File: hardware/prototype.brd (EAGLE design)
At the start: 62.2 x 57.2 mm, 32 parts, among them Q3 BS170

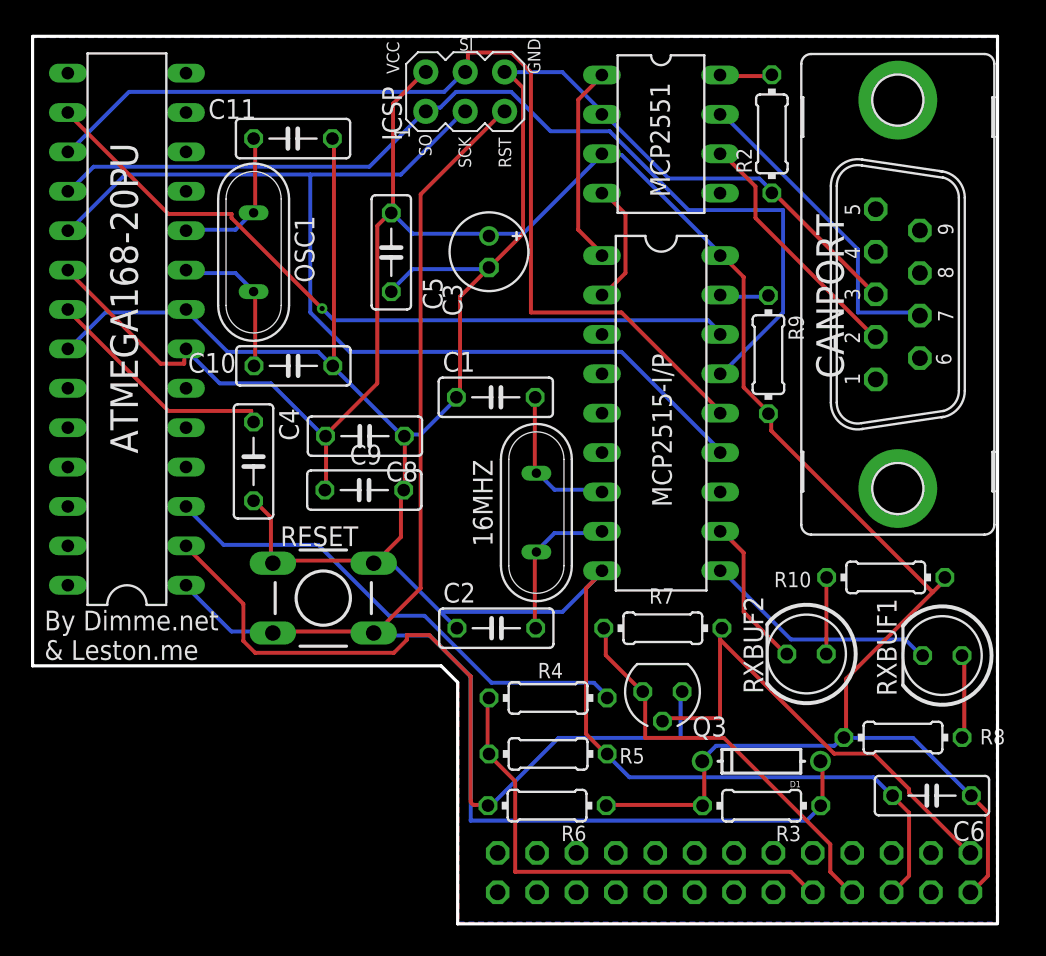
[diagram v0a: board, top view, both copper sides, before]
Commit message: Added gerbers for DirtyPCBs and OSHpark.
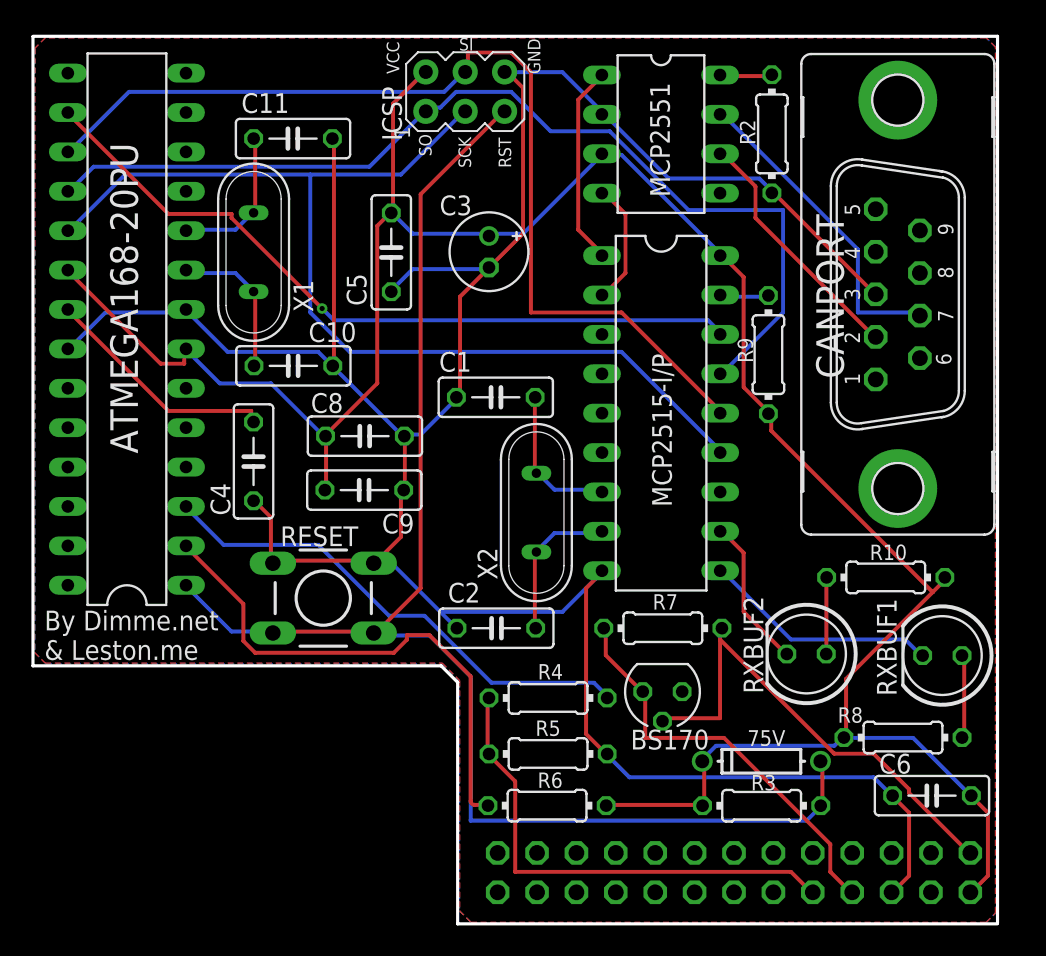
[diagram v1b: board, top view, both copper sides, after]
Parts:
- BS170: value BS170 -> (none)
- C1, C10, C11, C2: value (none) -> 22p
- C3: value (none) -> 10u
- C4, C5, C6, C8, C9: value (none) -> 100n
- R10, R8: value (none) -> 330
- R2: value (none) -> 4k7
- R3, R4, R5, R6, R7, R9: value (none) -> 10k
- X2: value (none) -> 16MHz
- renumbered 16MHZ to X2, D1 to 75V, OSC1 to X1, Q3 to BS170
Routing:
- net N$23: track 50.9 -> 33.6 mm
